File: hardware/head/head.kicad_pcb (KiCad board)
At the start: 2 copper layers, 80 x 55 mm, 58 parts, among them J1 Head bundle, J10 CM4 socket 101-200, J11 Ext amp, J12 Ext 5V, J2 ToF, J3 I2C breakout, J4 Eye LED, J5 Speaker, J6 Fan, J7 Microphone, J8 Camera, J9 CM4 socket 1-100, Q1 AO3400A, U2 LMR51635YDDCR, U3 AMS1117-3.3, U4 MAX98357AETE+T, U5 BMI088

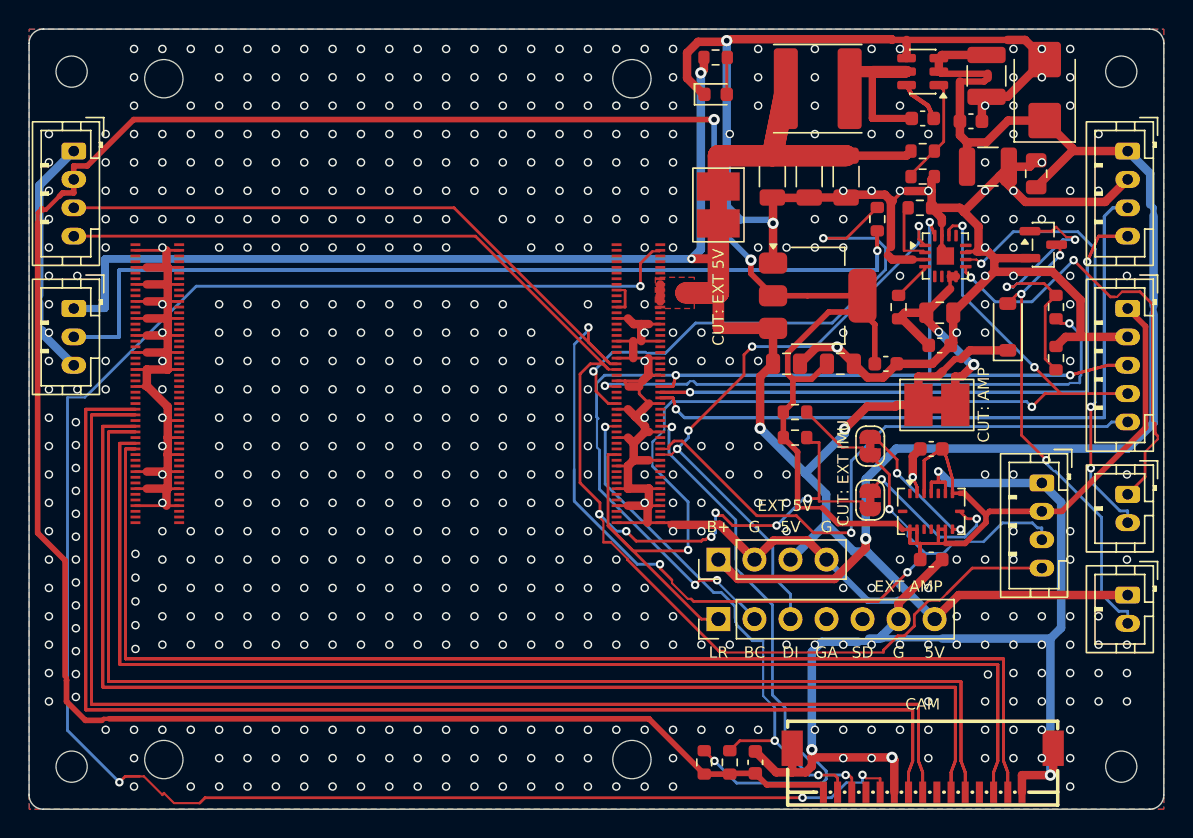
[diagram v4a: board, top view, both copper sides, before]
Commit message: Head carrier PCB: tidy the routing, sparser stitching
scripts/kicad/tidy_head_pcb.py removes the 610 stitching vias, replaces
pairs of segments meeting at a bare joint with one straight segment
where it clears other copper and the keep-outs (306 joints), widens
necked segments to their net class where they fit, and stitches again
on a 3.5 mm grid plus rows beside the camera pairs (163 vias). DRC with
schematic parity still clean. Fab package, renders and layout PDF
regenerated.
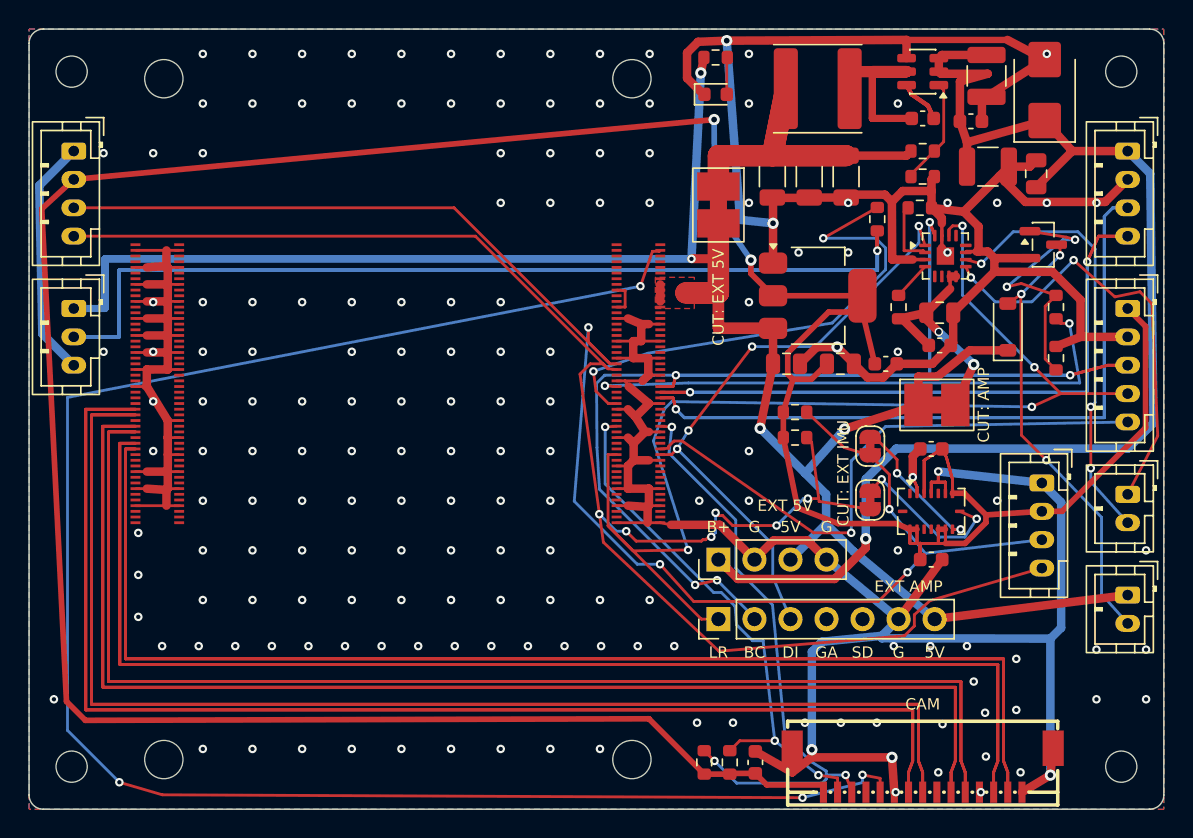
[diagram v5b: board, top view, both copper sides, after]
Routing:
- net GND: track 377.8 -> 371.8 mm, vias 618 -> 171
- net +3V3: track 258.9 -> 253.6 mm
- net /CAM_GPIO: track 132.6 -> 128.4 mm
- net /I2C8_SDA: track 112.4 -> 109.7 mm
- net /I2C8_SCL: track 122.3 -> 119.6 mm
- net +5V: track 204.4 -> 202.3 mm
- net /EYE_DATA: track 37.8 -> 36.3 mm
- net /SAI2_LRCK: track 83.5 -> 82.2 mm
- net /VBAT_IN: track 91.6 -> 90.6 mm
- net /FAN_G: track 19.7 -> 18.8 mm
- net /SAI2_SDO: track 43.6 -> 42.8 mm
- net /SAI2_SDI: track 42.2 -> 41.4 mm
- net /SPK_P: track 31.7 -> 30.9 mm
- net /CAM_SCL: track 43.2 -> 42.4 mm
- net /AMP_5V: track 17.6 -> 16.9 mm
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
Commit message: Head carrier PCB: remove the autorouter's redundant ground tracks
Freerouting routed GND as tracks before the pours existed; they showed
as copper across ground pads' thermal reliefs. All were ground on
ground. The tidy's new unground stage removes the 215 unlocked GND
segments; the pours reach every ground pad (C9's now solid). DRC with
schematic parity clean; fab package, renders and layout PDF
regenerated.
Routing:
- net GND: track 371.8 -> 9.12 mm

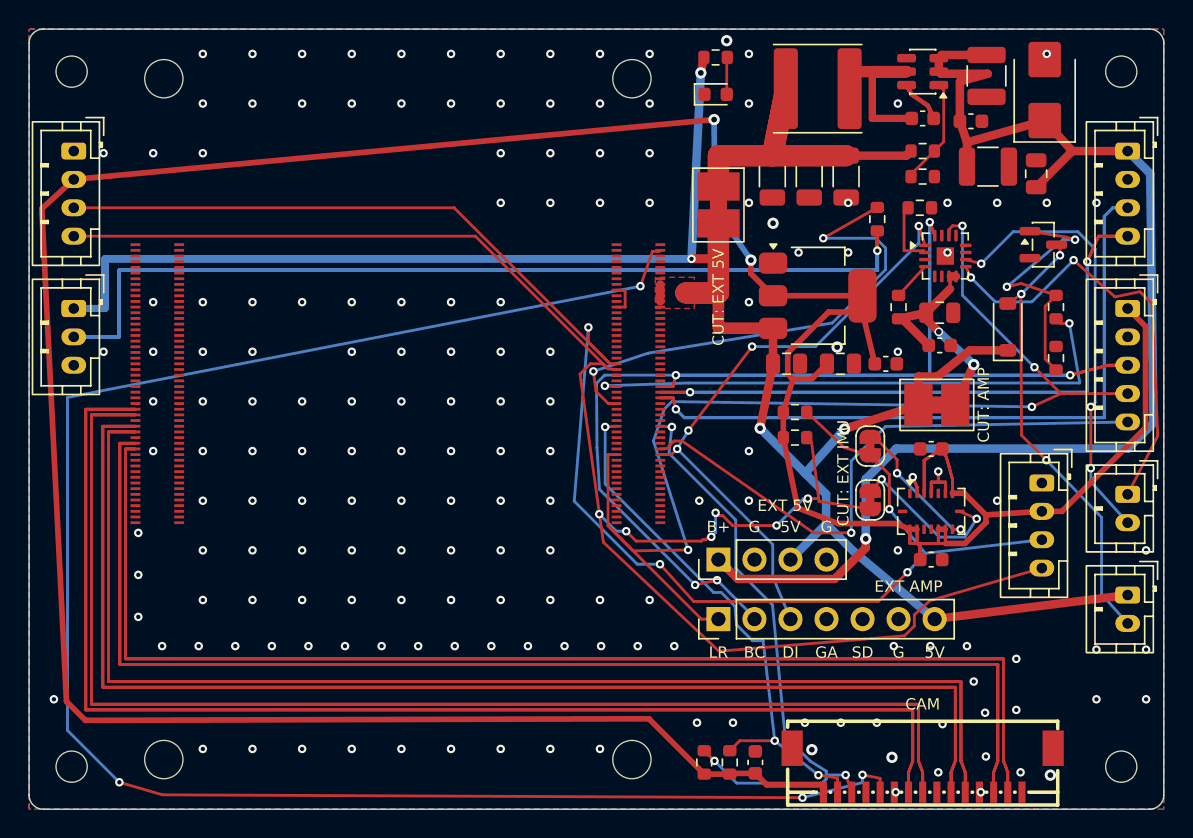
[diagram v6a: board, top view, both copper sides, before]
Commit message: Head carrier PCB: no vias in pads, duplicate tracks removed
The re-stitching had put five ground vias inside ground pads, among
them the amplifier's exposed pad; it now keeps clear of every pad.
The tidy's new dedupe stage removes the 97 copies Freerouting made of
the locked tracks, and straightening may now pass through a pad joint
when another track still reaches the pad. DRC with schematic parity
clean; fab package, renders and layout PDF regenerated.
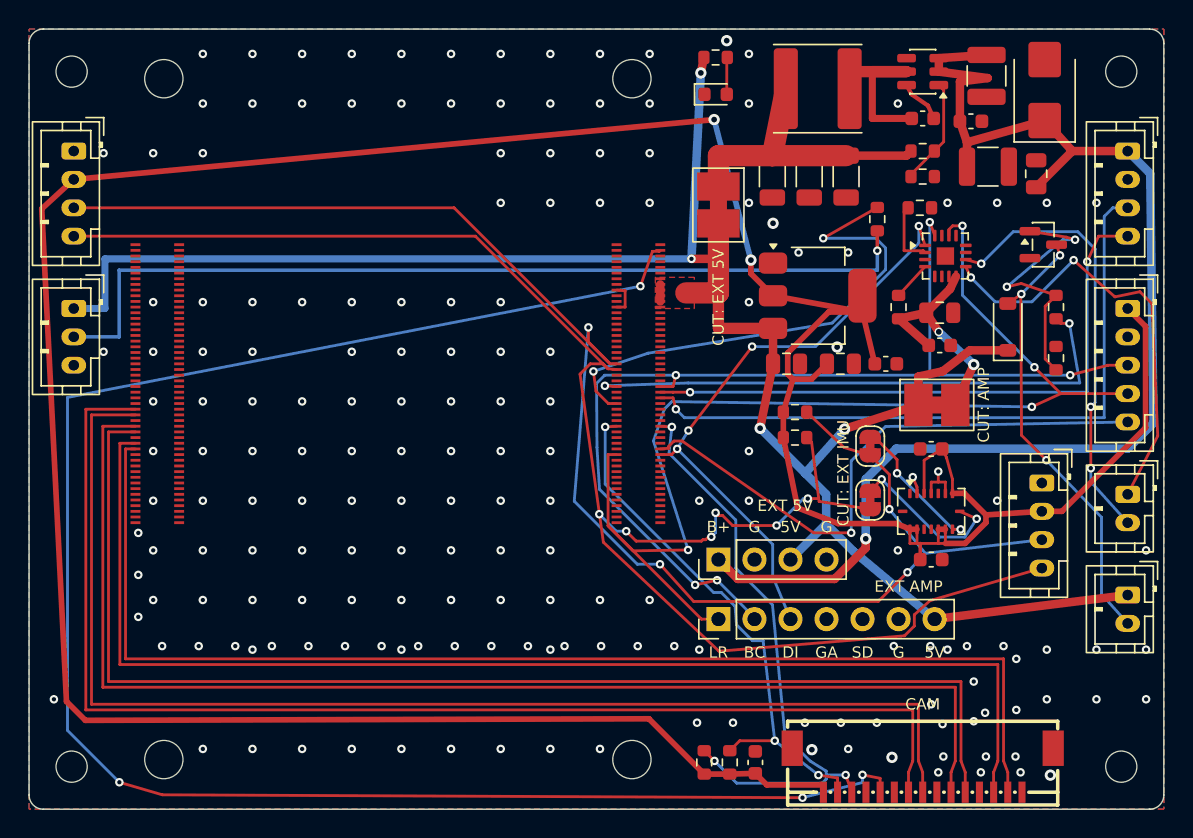
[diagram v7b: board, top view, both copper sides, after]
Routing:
- net /CSI_C_P: track 177.7 -> 88.9 mm
- net /CSI_D1_P: track 176.5 -> 88.3 mm
- net /CSI_C_N: track 176.1 -> 88.1 mm
- net /CSI_D0_P: track 175.3 -> 87.7 mm
- net /CSI_D1_N: track 174.9 -> 87.5 mm
- net /CSI_D0_N: track 173.7 -> 86.9 mm
- net /EYE_DIN: track 128.3 -> 64.1 mm
- net +5V: track 202.3 -> 139.7 mm
- net /UART7_RX: track 96.5 -> 48.3 mm
- net /SAI2_SCLK: track 119.2 -> 73.7 mm
- net /UART7_TX: track 86.6 -> 43.3 mm
- net +3V3: track 253.6 -> 237.3 mm
- net /5V_BUCK: track 39.3 -> 23.3 mm
- net /BUCK_SW: track 23.4 -> 12.5 mm
- net GND: track 9.12 -> 4.56 mm, vias 171 -> 182
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
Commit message: Head carrier PCB: SPI breakout pads (SPI2 M1) on the bottom
J13: nine wire pads under the module along the top edge (GND, 5V,
3V3, MOSI, MISO, CLK, CS0, INT, spare GPIO) on SPI2 M1, the RK3576 SPI
the eye LED leaves free, plus GPIO6 and GPIO5. The board is routed
again from placement with J13 in it; new scripts/kicad/sync_head_pcb.py
syncs a routed board with its schematic. The maze router now keeps
holes and footprint keep-outs clear, sees jumper bridges and uses
per-net clearances; the tidy gains an undangle stage and stitches
floating pour. DRC 0 violations; two module ground pins (J9 32, 33)
are boxed in and left unconnected, documented in docs/head-pcb.md 6.2.
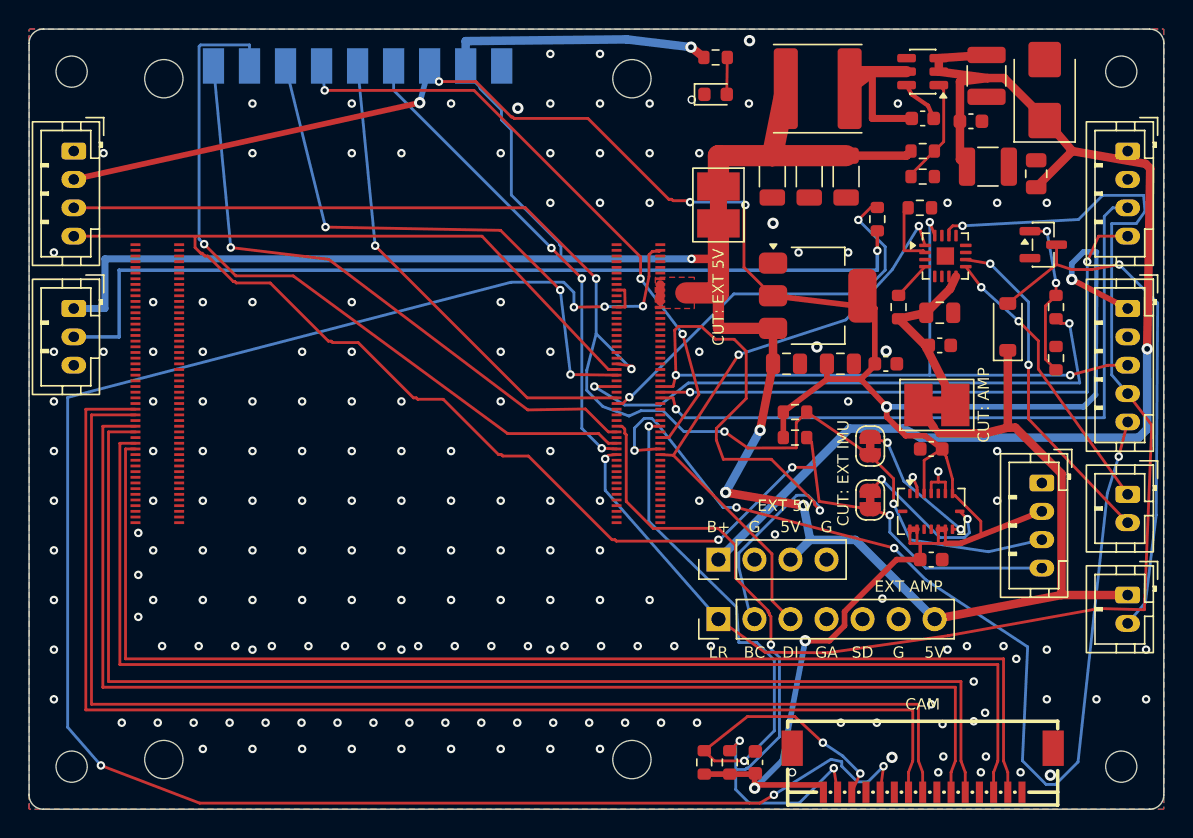
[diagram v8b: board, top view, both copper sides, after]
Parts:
- added J13: SPI pads, DukkiHead:SolderPads_1x09_P2.54mm_SPI, B.Cu at (133.3, 52.6)
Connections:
- J9 pad 28: unconnected-(J9-GPIO13-Pad28) -> /SPI2_MOSI
- J9 pad 30: unconnected-(J9-GPIO6-Pad30) -> /SPI_INT
- J9 pad 31: unconnected-(J9-GPIO12-Pad31) -> /SPI2_CLK
- J9 pad 34: unconnected-(J9-GPIO5-Pad34) -> /SPI_IO
- J9 pad 46: unconnected-(J9-GPIO22-Pad46) -> /SPI2_MISO
- J9 pad 54: unconnected-(J9-GPIO4-Pad54) -> /SPI2_CS0
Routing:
- net +3V3: track 237.3 -> 180.7 mm, vias 2 -> 8
- net /SPI_INT: track 0.00 -> 53.1 mm, vias 0 -> 1
- net /SPI_IO: track 0.00 -> 44.3 mm, vias 0 -> 1
- net /SPI2_CLK: track 0.00 -> 44.0 mm, vias 0 -> 3
- net /SPI2_CS0: track 0.00 -> 39.4 mm, vias 0 -> 3
- net /SPI2_MISO: track 0.00 -> 34.2 mm, vias 0 -> 1
- net /SPI2_MOSI: track 0.00 -> 34.1 mm, vias 0 -> 3
- net /SAI2_SDI: track 41.4 -> 74.7 mm, vias 1 -> 4
- net +5V: track 139.7 -> 170.9 mm, vias 4 -> 5
- net /I2C8_SDA: track 109.7 -> 92.8 mm
- net /SAI2_LRCK: track 82.2 -> 93.4 mm, vias 4 -> 2
- net /SPK_P: track 30.9 -> 20.2 mm
- net /SAI2_SCLK: track 73.7 -> 84.3 mm, vias 5 -> 4
- net /CAM_SDA: track 38.1 -> 47.8 mm
- net /EYE_DATA: track 36.3 -> 28.9 mm
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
